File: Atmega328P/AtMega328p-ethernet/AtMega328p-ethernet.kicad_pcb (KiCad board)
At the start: 2 copper layers, 75 parts, among them J1 Conn_01x05_Socket, J2 USB_C_Receptacle_USB2.0_16P, J3 RJ45_Abracon_ARJP11A-MASA-B-A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, J4 Conn_01x06_Socket, J5 Conn_01x06_Socket, J6 Conn_01x06_Socket, J7 Conn_01x04_Socket, J8 Conn_02x03_Counter_Clockwise, SW1 SW_Push, U1 ATmega328P-A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

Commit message: PCB Layout done initial
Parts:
- J1: footprint Connector_PinHeader_1.27mm:PinHeader_1x05_P1.27mm_Vertical -> Connector_PinHeader_2.54mm:PinHeader_1x05_P2.54mm_Vertical
- J4, J5, J6: footprint Connector_PinHeader_1.27mm:PinHeader_1x06_P1.27mm_Vertical -> Connector_PinHeader_2.54mm:PinHeader_1x06_P2.54mm_Vertical
- J7: value Conn_01x04_Socket -> Conn_01x06_Socket; footprint Connector_PinHeader_1.27mm:PinHeader_1x04_P1.27mm_Vertical -> Connector_PinHeader_2.54mm:PinHeader_1x06_P2.54mm_Vertical
- J8: footprint Connector_PinHeader_1.27mm:PinHeader_2x03_P1.27mm_Vertical -> Connector_PinHeader_2.54mm:PinHeader_2x03_P2.54mm_Vertical
- TP1, TP2, TP3, TP4: footprint TestPoint:TestPoint_Pad_D4.0mm -> TestPoint:TestPoint_Pad_1.0x1.0mm
- moved C3 100.1 mm to (145.5, 142.0), turned to -90 degrees
- moved C4 97.3 mm to (143.5, 142.0), turned to 90 degrees
- moved C1 96.8 mm to (141.5, 136.8), turned to 90 degrees
- moved J6 96.2 mm to (163.2, 146.5), turned to -90 degrees
- moved C2 95.5 mm to (138.0, 137.5), turned to 90 degrees
- moved J5 94.0 mm to (145.0, 146.5), turned to -90 degrees
- moved R2 93.7 mm to (150.5, 142.0), turned to 90 degrees
- moved D1 92.3 mm to (150.5, 138.7), turned to 90 degrees
- moved R3 91.7 mm to (152.5, 142.0), turned to 90 degrees
- moved D2 89.8 mm to (152.5, 138.7), turned to 90 degrees
- moved U1 86.8 mm to (147.0, 131.5), turned to 45 degrees
- moved R1 82.9 mm to (134.0, 131.0), turned to 180 degrees
- moved J2 79.1 mm to (101.5, 140.0), turned to -90 degrees
- moved C14 78.7 mm to (138.0, 116.0), turned to -90 degrees
- moved J1 78.1 mm to (163.0, 129.0)
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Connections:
- net Net-(J3-RD+) renamed /ETHERNET_MODULE/ETH_RXP_C
- net Net-(J3-RD-) renamed /ETHERNET_MODULE/ETH_RXN_C
- net Net-(J3-TD+) renamed /ETHERNET_MODULE/ETH_TXP_C
- net Net-(J3-TD-) renamed /ETHERNET_MODULE/ETH_TXN_C
- net Net-(U2-RXN) renamed /ETHERNET_MODULE/ETH_RXN
- net Net-(U2-RXP) renamed /ETHERNET_MODULE/ETH_RXP
- net Net-(U2-TXN) renamed /ETHERNET_MODULE/ETH_TXN
- net Net-(U2-TXP) renamed /ETHERNET_MODULE/ETH_TXP
- R5 pad 1: I2C_SDA -> /I2C_SDA
- R6 pad 1: I2C_SCL -> /I2C_SCL
- U1 pad 27: I2C_SDA -> /I2C_SDA
- U1 pad 28: I2C_SCL -> /I2C_SCL
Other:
- board outline added: 66.5 x 50 mm
- copper layers 2 -> 4

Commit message: Added lots of lcsc part numbers
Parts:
- added R22: 56k, Resistor_SMD:R_0603_1608Metric, F.Cu at (109.2, 146.0)
- added R23: 56k, Resistor_SMD:R_0603_1608Metric, F.Cu at (109.2, 148.5)
- J2: footprint Connector_USB:USB_C_Receptacle_Amphenol_124019772112A -> Connector_USB:USB_C_Receptacle_G-Switch_GT-USB-7010ASV
- moved J2 0.95 mm to (102.5, 140.0)
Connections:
- net Net-(U3-D+) renamed /USB_INTERFACE/USB_P
- net Net-(U3-D-) renamed /USB_INTERFACE/USB_N
- J2 pad A5: unconnected-(J2-CC1-PadA5) -> Net-(J2-CC1)
- J2 pad B5: unconnected-(J2-CC2-PadB5) -> Net-(J2-CC2)
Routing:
- net /USB_INTERFACE/USB_P: track 0.00 -> 6.95 mm
- net /USB_INTERFACE/USB_N: track 0.00 -> 6.95 mm

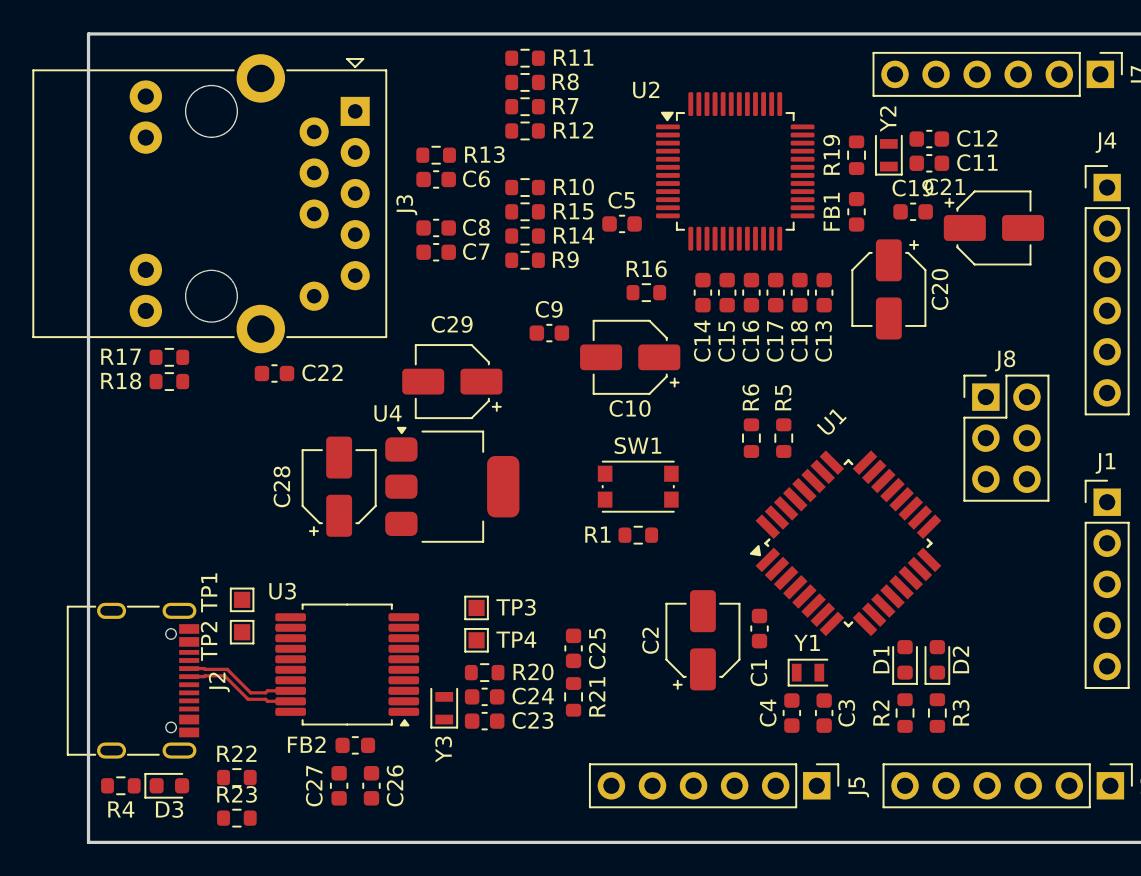
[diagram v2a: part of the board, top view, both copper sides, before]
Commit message: Most components selected using lcsc
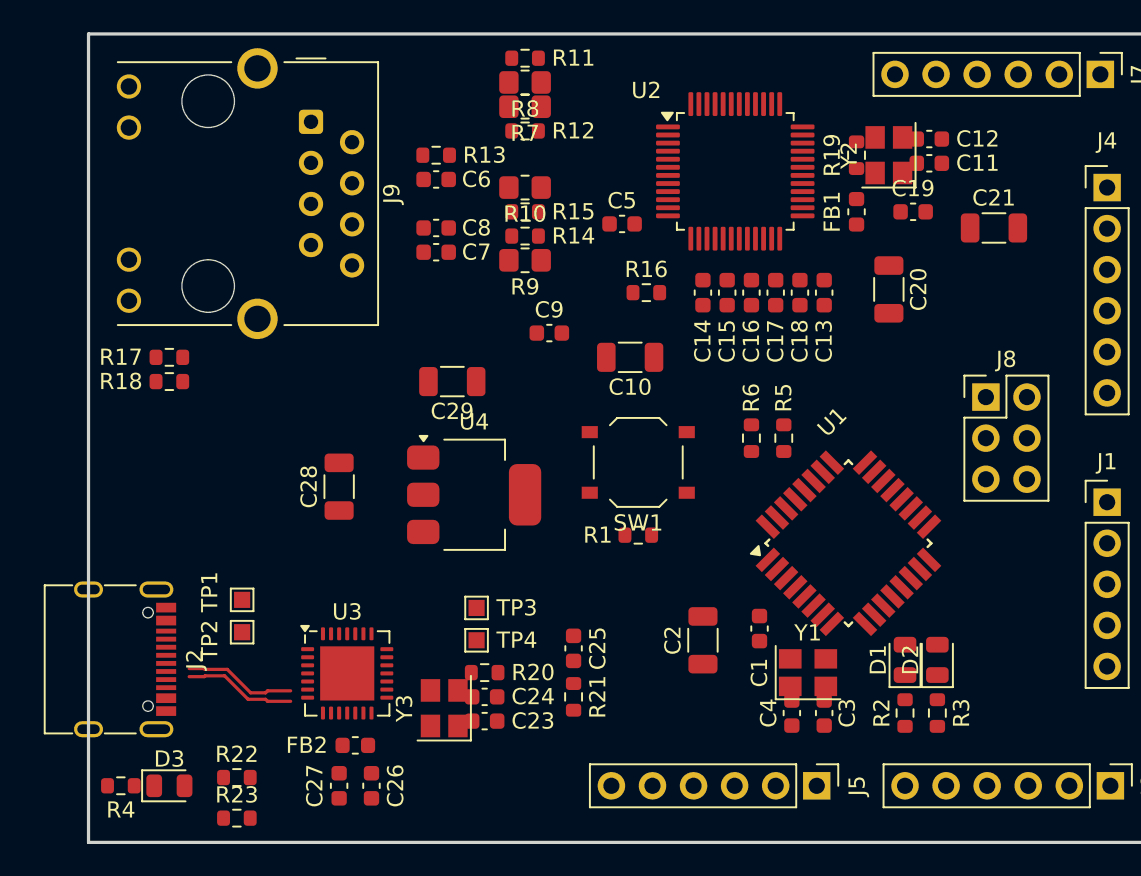
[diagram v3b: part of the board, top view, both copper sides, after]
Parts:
- removed C22: 1nF/2kV, Capacitor_SMD:C_0603_1608Metric
- removed J3: RJ45_Abracon_ARJP11A-MASA-B-A-EMU2, Connector_RJ:RJ45_Abracon_ARJP11A-MA_Horizontal
- added J9: RJ45_Hanrun_HR911105A_Horizontal, Connector_RJ:RJ45_Hanrun_HR911105A_Horizontal, F.Cu at (113.8, 105.4)
- C10, C2, C20, C21, C28, C29: footprint Capacitor_SMD:CP_Elec_4x3 -> Capacitor_SMD:C_1206_3216Metric
- D1, D3: value LED -> LED-GREEN; footprint LED_SMD:LED_0603_1608Metric -> LED_SMD:LED_0805_2012Metric
- D2: value LED -> LED-RED; footprint LED_SMD:LED_0603_1608Metric -> LED_SMD:LED_0805_2012Metric
- FB1, FB2: value HH-1M1608-121JT -> 100R@100MHz
- J2: value USB_C_Receptacle_USB2.0_16P -> USB_C_Receptacle_USB2.0_12P
- R1: value R_Small -> 4.7k
- R10, R7, R8, R9: footprint Resistor_SMD:R_0603_1608Metric -> Resistor_SMD:R_0805_2012Metric_Pad1.20x1.40mm_HandSolder
- SW1: footprint Button_Switch_SMD:SW_Push_1P1T_NO_CK_KMR2 -> Button_Switch_SMD:SW_Push_1P1T_XKB_TS-1187A
- U3: value MCP2200-I-SS -> CP2102N-Axx-xQFN28; footprint Package_SO:SSOP-20_5.3x7.2mm_P0.65mm -> Package_DFN_QFN:QFN-28-1EP_5x5mm_P0.5mm_EP3.35x3.35mm
- U4: value NCP1117-3.3_SOT223 -> AMS1117-3.3
- Y1, Y2, Y3: footprint Crystal:Crystal_SMD_2012-2Pin_2.0x1.2mm -> Crystal:Crystal_SMD_3225-4Pin_3.2x2.5mm
- moved J2 1.94 mm to (101.1, 138.7)
- moved SW1 1.50 mm to (134.0, 126.5)
- moved U4 1.44 mm to (123.8, 128.5)
- moved U3 0.55 mm to (116.0, 139.6), turned to 0 degrees
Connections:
- R20 pad 1: Net-(U3-RST) -> unconnected-(R20-Pad1)
- TP1 pad 1: Net-(U3-GP1/USB-CFG) -> unconnected-(TP1-Pad1)
- TP2 pad 1: Net-(U3-GP0/SSPND) -> unconnected-(TP2-Pad1)
- TP3 pad 1: Net-(U3-GP6/RxLED) -> unconnected-(TP3-Pad1)
- TP4 pad 1: Net-(U3-GP7/TxLED) -> unconnected-(TP4-Pad1)
- U2 pad 14: Net-(U2-AGND-Pad14) -> GND
- U2 pad 16: Net-(U2-AGND-Pad14) -> GND
- U2 pad 19: Net-(U2-AGND-Pad14) -> GND
- U2 pad 29: unconnected-(U2-GND-Pad29) -> GND
- U2 pad 3: Net-(U2-AGND-Pad14) -> GND
- U2 pad 48: Net-(U2-AGND-Pad14) -> GND
- U2 pad 9: Net-(U2-AGND-Pad14) -> GND
- U3 pad 1: +5V -> unconnected-(U3-~{DCD}-Pad1)
- U3 pad 10: /MCU_RXD -> unconnected-(U3-NC-Pad10)
- U3 pad 12: /MCU_TXD -> unconnected-(U3-SUSPEND-Pad12)
- U3 pad 13: GND -> unconnected-(U3-CHREN-Pad13)
- U3 pad 15: Net-(U3-GP1/USB-CFG) -> unconnected-(U3-CHR0-Pad15)
- U3 pad 16: Net-(U3-GP0/SSPND) -> unconnected-(U3-~{WAKEUP}/GPIO.3-Pad16)
- U3 pad 17: VBUS -> unconnected-(U3-RS485/GPIO.2-Pad17)
- U3 pad 18: /USB_INTERFACE/USB_N -> unconnected-(U3-~{RXT}/GPIO.1-Pad18)
- U3 pad 19: /USB_INTERFACE/USB_P -> unconnected-(U3-~{TXT}/GPIO.0-Pad19)
- U3 pad 2: /USB_INTERFACE/OSC1 -> unconnected-(U3-~{RI}/CLK-Pad2)
- U3 pad 20: GND -> unconnected-(U3-GPIO.6-Pad20)
- U3 pad 3: /USB_INTERFACE/OSC2 -> Net-(U3-GND-Pad29)
- U3 pad 4: Net-(U3-RST) -> unconnected-(U3-D+-Pad4)
- U3 pad 5: Net-(U3-GP7/TxLED) -> unconnected-(U3-D--Pad5)
- U3 pad 6: Net-(U3-GP6/RxLED) -> unconnected-(U3-VDD-Pad6)

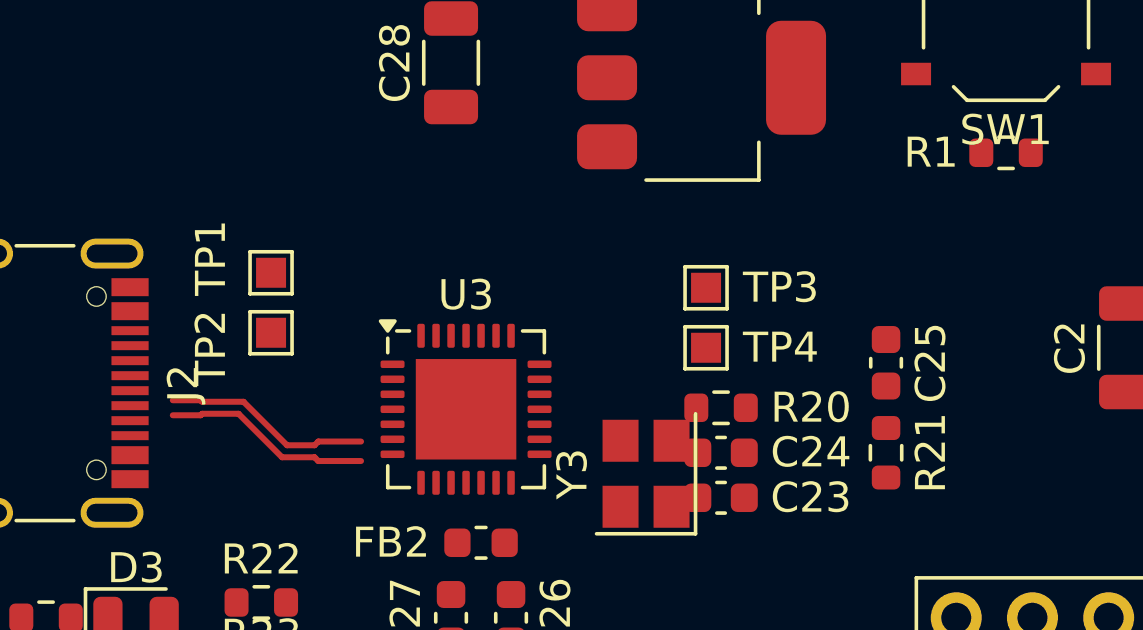
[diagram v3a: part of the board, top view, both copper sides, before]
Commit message: All parts matching lcsc replaced usb transever
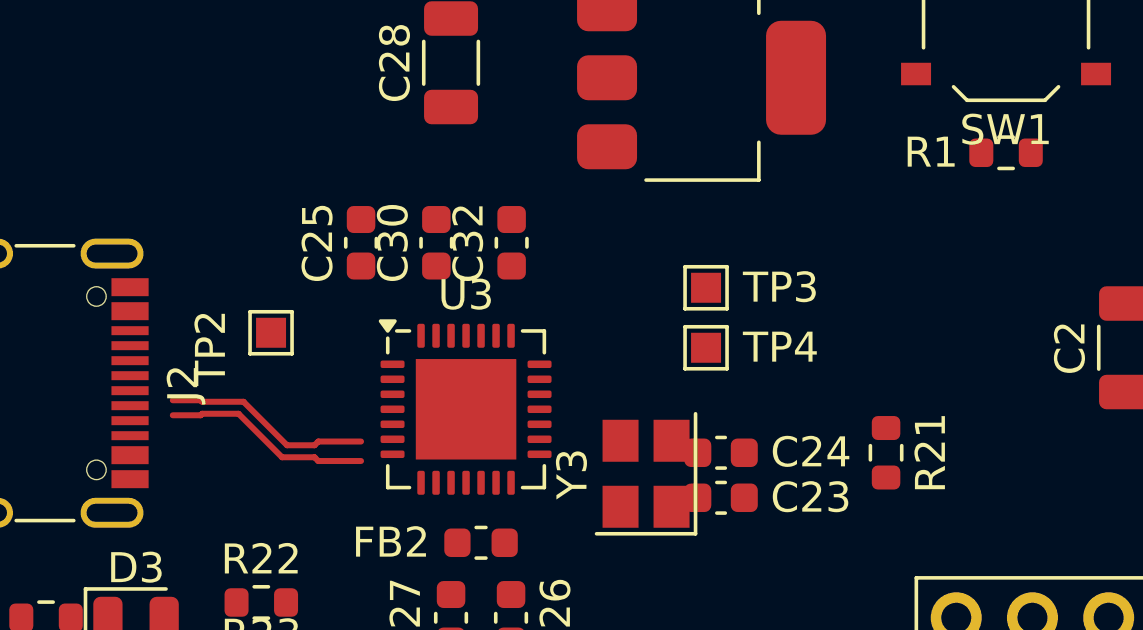
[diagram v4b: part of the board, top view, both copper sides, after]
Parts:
- removed R20: 470R, Resistor_SMD:R_0603_1608Metric
- removed TP1: USBCFG, TestPoint:TestPoint_Pad_1.0x1.0mm
- added C30: 4.7uF, Capacitor_SMD:C_0603_1608Metric, F.Cu at (115.0, 134.0)
- added C32: 100nF, Capacitor_SMD:C_0603_1608Metric, F.Cu at (117.5, 134.0)
- R21: value 10k -> 1k
- moved C25 18.0 mm to (112.5, 134.0)
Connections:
- C25 pad 1: Net-(C25-Pad1) -> VBUS
- R21 pad 1: Net-(C25-Pad1) -> Net-(U3-~{RST})
- TP2 pad 1: unconnected-(TP2-Pad1) -> Net-(U3-SUSPEND)
- TP3 pad 1: unconnected-(TP3-Pad1) -> Net-(U3-~{RXT}/GPIO.1)
- TP4 pad 1: unconnected-(TP4-Pad1) -> Net-(U3-~{TXT}/GPIO.0)
- U3 pad 12: unconnected-(U3-SUSPEND-Pad12) -> Net-(U3-SUSPEND)
- U3 pad 18: unconnected-(U3-~{RXT}/GPIO.1-Pad18) -> Net-(U3-~{RXT}/GPIO.1)
- U3 pad 19: unconnected-(U3-~{TXT}/GPIO.0-Pad19) -> Net-(U3-~{TXT}/GPIO.0)
- U3 pad 25: unconnected-(U3-RXD-Pad25) -> /MCU_TXD
- U3 pad 26: unconnected-(U3-TXD-Pad26) -> /MCU_RXD
- U3 pad 29: Net-(U3-GND-Pad29) -> GND
- U3 pad 3: Net-(U3-GND-Pad29) -> GND
- U3 pad 4: unconnected-(U3-D+-Pad4) -> /USB_INTERFACE/USB_P
- U3 pad 5: unconnected-(U3-D--Pad5) -> /USB_INTERFACE/USB_N
- U3 pad 6: unconnected-(U3-VDD-Pad6) -> Net-(U3-VDD)
- U3 pad 7: unconnected-(U3-VREGIN-Pad7) -> VBUS
- U3 pad 8: unconnected-(U3-VBUS-Pad8) -> VBUS
- U3 pad 9: unconnected-(U3-~{RST}-Pad9) -> Net-(U3-~{RST})

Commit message: Continued cleanup
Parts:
- removed C23, C24: 18pF, Capacitor_SMD:C_0603_1608Metric
- removed Y3: 12MHz, Crystal:Crystal_SMD_3225-4Pin_3.2x2.5mm
- added C22: 1000pF, Capacitor_SMD:C_0603_1608Metric, F.Cu at (128.9, 154.4)
- added R20: 0R, Resistor_SMD:R_0805_2012Metric_Pad1.20x1.40mm_HandSolder, F.Cu at (124.5, 154.6)
- added R24: 0R, Resistor_SMD:R_0805_2012Metric_Pad1.20x1.40mm_HandSolder, F.Cu at (124.5, 157.6)
- added R25: 0R, Resistor_SMD:R_0805_2012Metric_Pad1.20x1.40mm_HandSolder, F.Cu at (124.5, 160.5)
- J1: value Conn_01x05_Socket -> Conn_01x06_Socket; footprint Connector_PinHeader_2.54mm:PinHeader_1x05_P2.54mm_Vertical -> Connector_PinHeader_2.54mm:PinHeader_1x06_P2.54mm_Vertical
- R16: footprint Resistor_SMD:R_0603_1608Metric -> Resistor_SMD:R_0603_1608Metric_Pad0.98x0.95mm_HandSolder
- moved FB1 40.8 mm to (124.2, 144.5), turned to 0 degrees
- moved FB2 8.28 mm to (124.2, 147.0)
- moved C26 8.09 mm to (124.2, 142.0), turned to 0 degrees
- moved J2 1.34 mm to (102.4, 138.9)
- moved J1 1.16 mm to (163.0, 127.8)
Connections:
- C13 pad 1: +3.3VA -> /ETHERNET_MODULE/+3.3VA_IN
- C14 pad 1: +3.3VA -> /ETHERNET_MODULE/+3.3VA_IN
- C15 pad 1: +3.3VA -> /ETHERNET_MODULE/+3.3VA_IN
- C16 pad 1: +3.3VA -> /ETHERNET_MODULE/+3.3VA_IN
- C17 pad 1: +3.3VA -> /ETHERNET_MODULE/+3.3VA_IN
- C18 pad 1: +3.3VA -> /ETHERNET_MODULE/+3.3VA_IN
- C20 pad 1: +3.3VA -> /ETHERNET_MODULE/+3.3VA_IN
- FB1 pad 1: +3.3V -> /ETHERNET_MODULE/+3.3VA_IN
- FB1 pad 2: +3.3VA -> +3.3V
- J9 pad 8: GND -> Net-(C22-Pad1)
- J9 pad SH: GND -> Net-(C22-Pad1)
- R11 pad 2: +3.3VA -> /ETHERNET_MODULE/+3.3VA_IN
- R12 pad 2: +3.3VA -> /ETHERNET_MODULE/+3.3VA_IN
- R13 pad 2: +3.3VA -> /ETHERNET_MODULE/+3.3VA_IN
- R21 pad 2: +5V -> VBUS
- U1 pad 14: /ETH_SPI_SS -> GND
- U2 pad 11: +3.3VA -> /ETHERNET_MODULE/+3.3VA_IN
- U2 pad 15: +3.3VA -> /ETHERNET_MODULE/+3.3VA_IN
- U2 pad 17: +3.3VA -> /ETHERNET_MODULE/+3.3VA_IN
- U2 pad 21: +3.3VA -> /ETHERNET_MODULE/+3.3VA_IN
- U2 pad 35: /ETH_SPI_SS -> GND
- U2 pad 4: +3.3VA -> /ETHERNET_MODULE/+3.3VA_IN
- U2 pad 43: unconnected-(U2-PMODE2-Pad43) -> Net-(U2-PMODE2)
- U2 pad 44: unconnected-(U2-PMODE1-Pad44) -> Net-(U2-PMODE1)
- U2 pad 45: unconnected-(U2-PMODE0-Pad45) -> Net-(U2-PMODE0)
- U2 pad 8: +3.3VA -> /ETHERNET_MODULE/+3.3VA_IN
- Y1 pad 2: /XTAL2 -> unconnected-(Y1-Pad2)
- Y1 pad 3: (no net) -> /XTAL2
- Y1 pad 4: (no net) -> unconnected-(Y1-Pad4)
- Y2 pad 2: /ETHERNET_MODULE/XO -> unconnected-(Y2-Pad2)
- Y2 pad 3: (no net) -> /ETHERNET_MODULE/XO
- Y2 pad 4: (no net) -> unconnected-(Y2-Pad4)
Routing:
- added copper zone on In2.Cu, net +5V
- added copper zone on In1.Cu, net GND

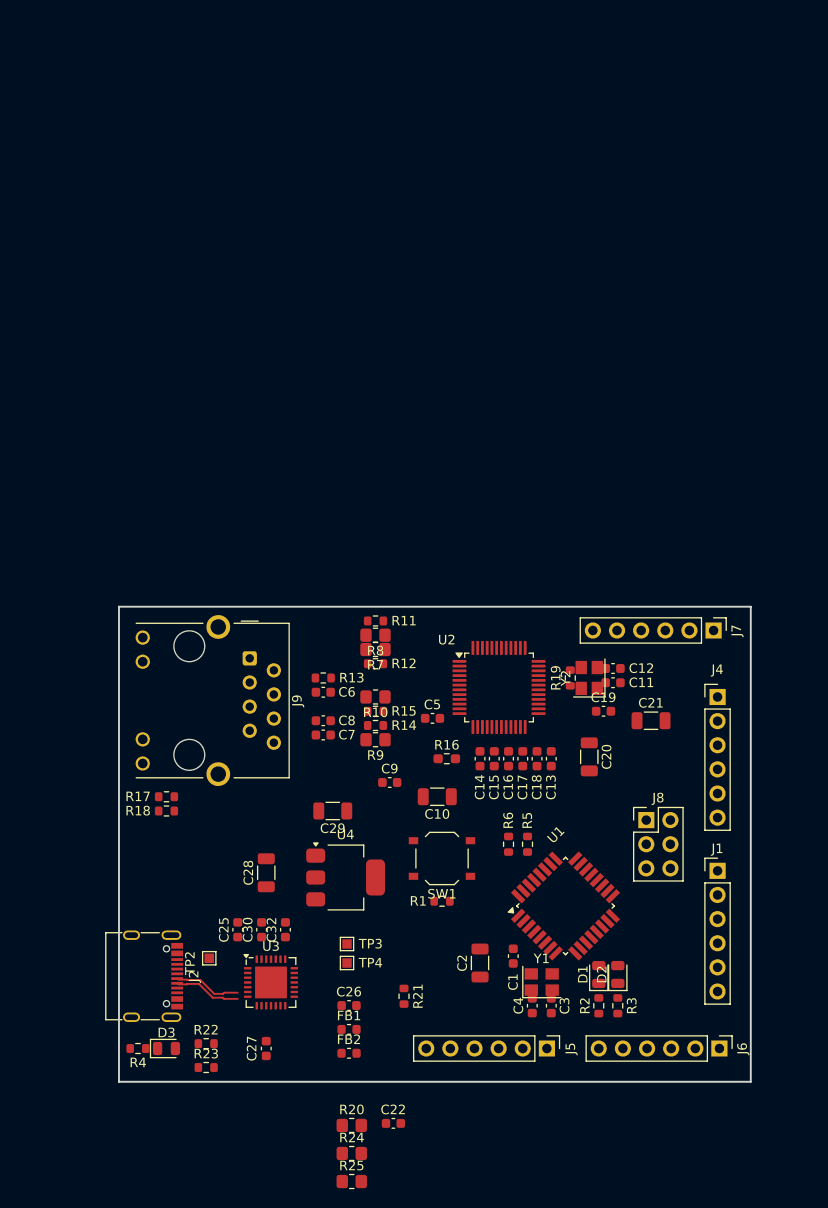
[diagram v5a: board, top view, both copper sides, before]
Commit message: USB and microcontroller layed out
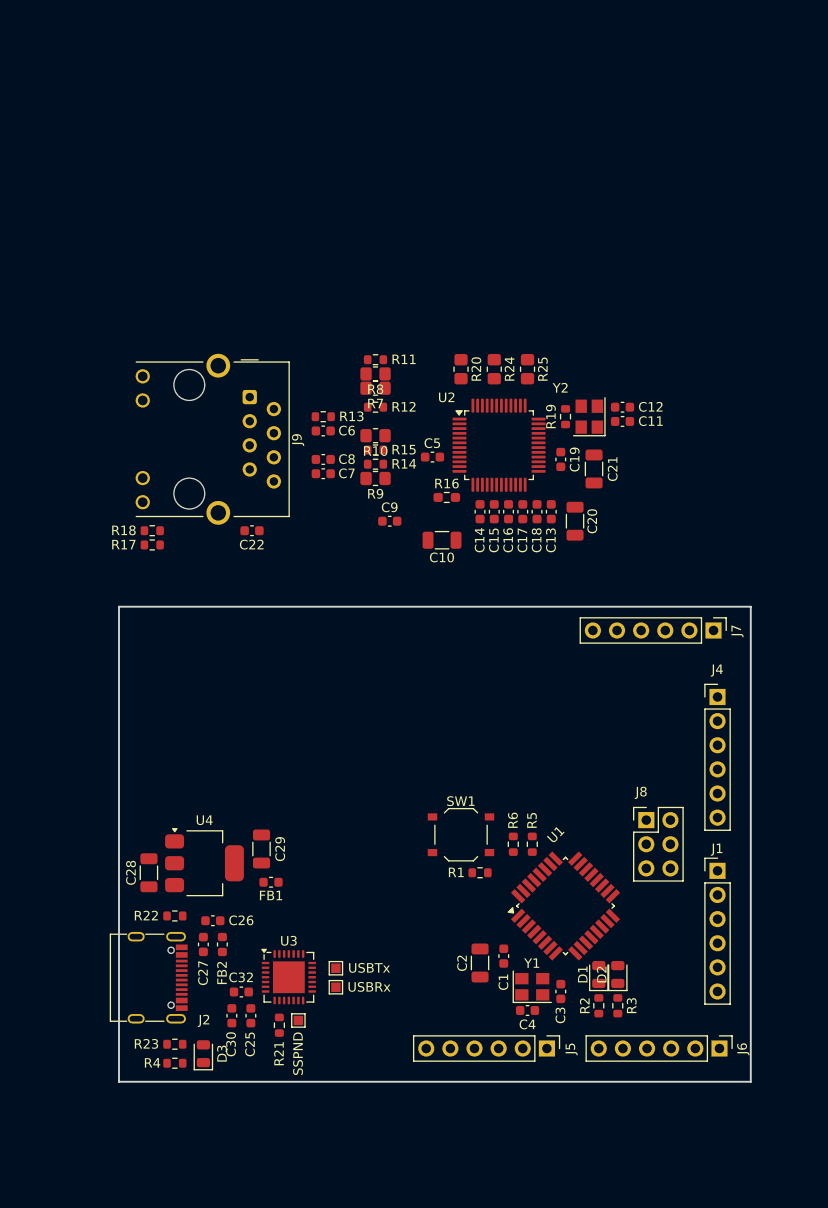
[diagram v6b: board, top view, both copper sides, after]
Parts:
- R22, R23: value 56k -> 5.1k
- moved R25 87.5 mm to (143.0, 75.0), turned to -90 degrees
- moved R24 83.9 mm to (139.5, 75.0), turned to -90 degrees
- moved R20 80.4 mm to (136.0, 75.0), turned to -90 degrees
- moved C22 64.1 mm to (114.0, 92.0)
- moved R18 29.5 mm to (103.5, 92.0)
- moved C11 27.5 mm to (153.0, 80.5)
- moved C12 27.5 mm to (153.0, 79.0)
- moved R19 27.5 mm to (147.0, 80.0)
- moved C5 27.5 mm to (133.0, 84.2)
- moved C6 27.5 mm to (121.5, 81.5)
- moved C7 27.5 mm to (121.5, 86.0)
- moved C8 27.5 mm to (121.5, 84.5)
- moved C9 27.5 mm to (128.5, 91.0)
- moved J9 27.5 mm to (113.8, 77.9)
- moved R10 27.5 mm to (127.0, 82.0)
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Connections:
- R22 pad 1: Net-(J2-CC1) -> GND
- R22 pad 2: VBUS -> Net-(J2-CC1)
- R23 pad 1: Net-(J2-CC2) -> GND
- R23 pad 2: VBUS -> Net-(J2-CC2)
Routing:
- net /USB_INTERFACE/USB_P: track 6.95 -> 0.00 mm
- net /USB_INTERFACE/USB_N: track 6.95 -> 0.00 mm
